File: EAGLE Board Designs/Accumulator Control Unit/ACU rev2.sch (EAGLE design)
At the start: 100 parts, among them J1 CONNECTOR-CAN_NF_T_V_BLACK, J2 CONNECTOR-6_MF_T_V_, J3 CONNECTOR-8_MF_T_V_, Q1 TRANSISTOR_N_MOS__PMV15ENEA, U1 VOLTAGE_REGULATOR_SOT89_12V, U10 OPAMP_1_CHANNEL_OPA991, U11 LOGICGATE_AND_DCK3, U12 OPAMP_1_CHANNEL_OPA991, U13 OPAMP_1_CHANNEL_OPA991, U14 OPAMP_1_CHANNEL_OPA991, U15 LOGICGATE_AND_DCK3, U16 OPAMP_1_CHANNEL_OPA991, U17 OPAMP_1_CHANNEL_OPA991, U18 OPAMP_1_CHANNEL_OPA991, U2 ADG1423, U3 LM555, U4 OPAMP_1_CHANNEL_OPA991, U5 MAX7404, U6 MAX7404, U7 OPAMP_1_CHANNEL_OPA991, U8 LOGICGATE_AND_DCK3, U9 OPAMP_1_CHANNEL_OPA991

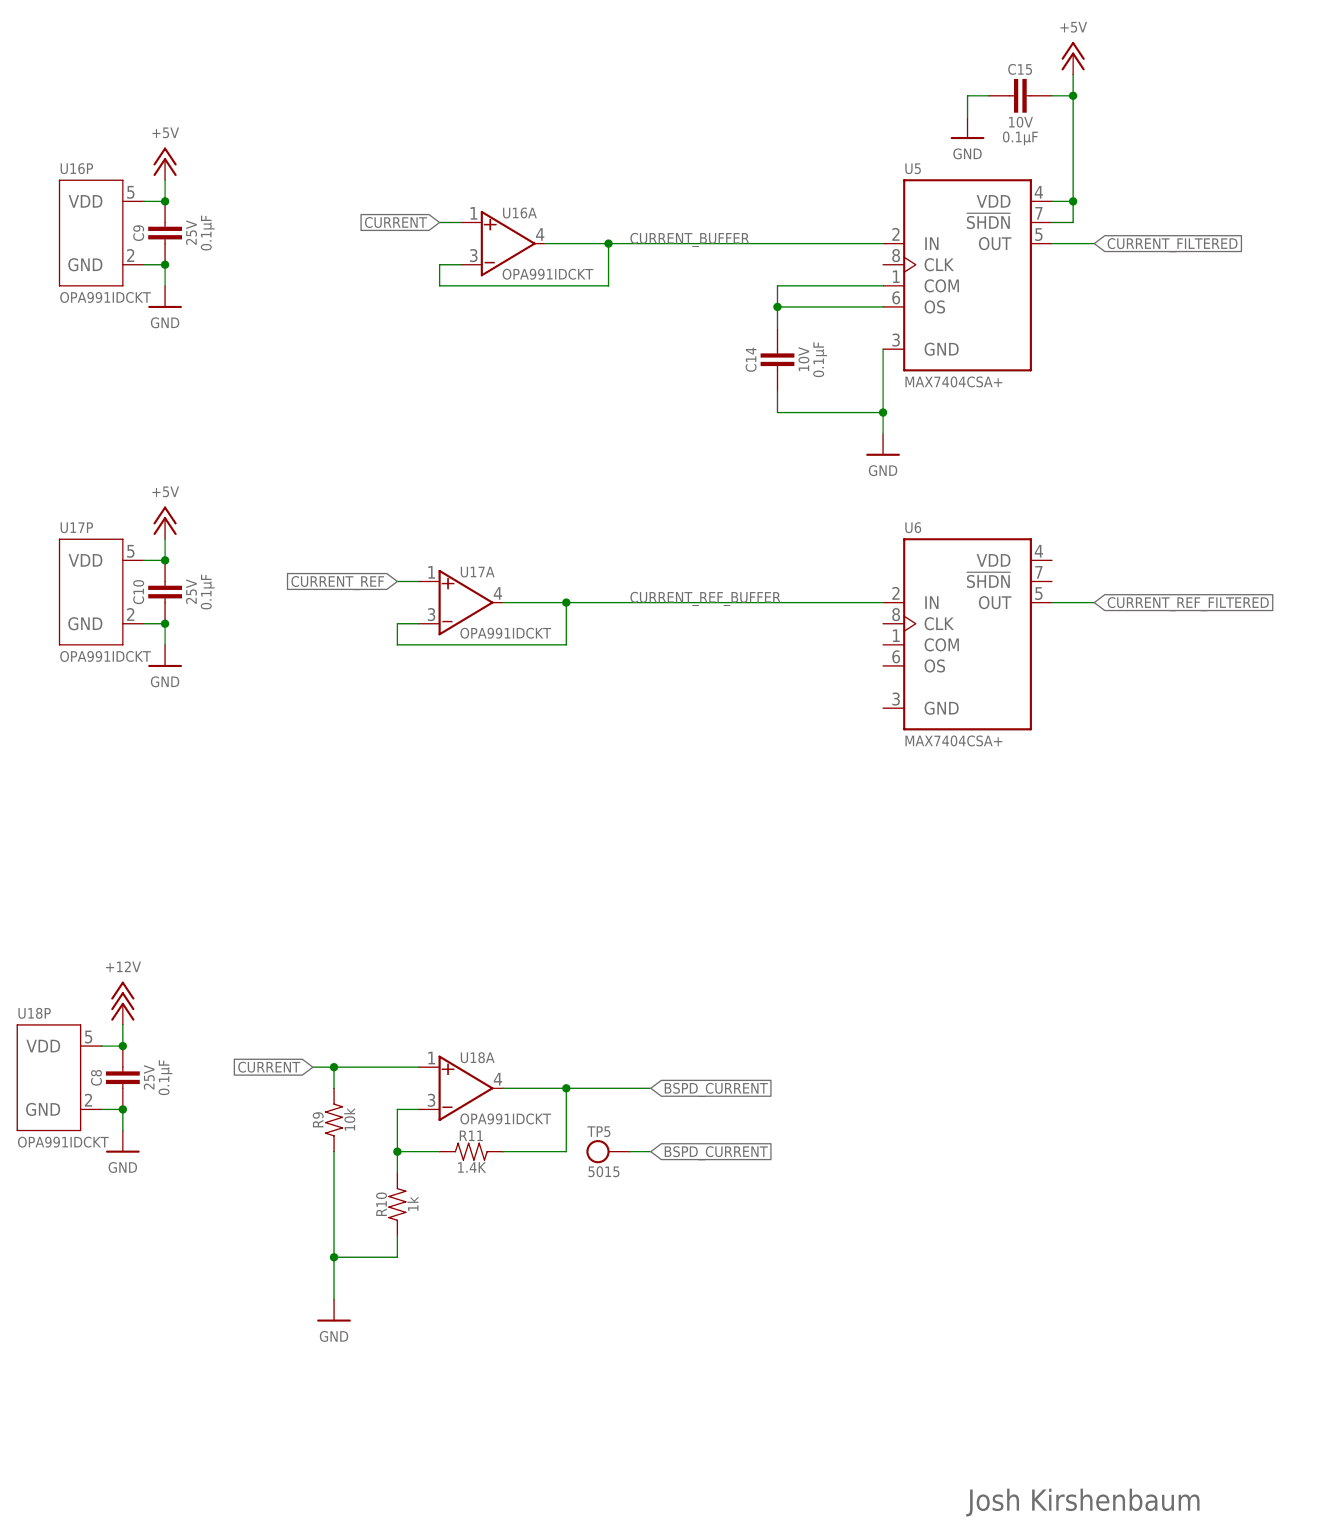
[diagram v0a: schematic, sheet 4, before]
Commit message: filtering capacitor and tvs diode
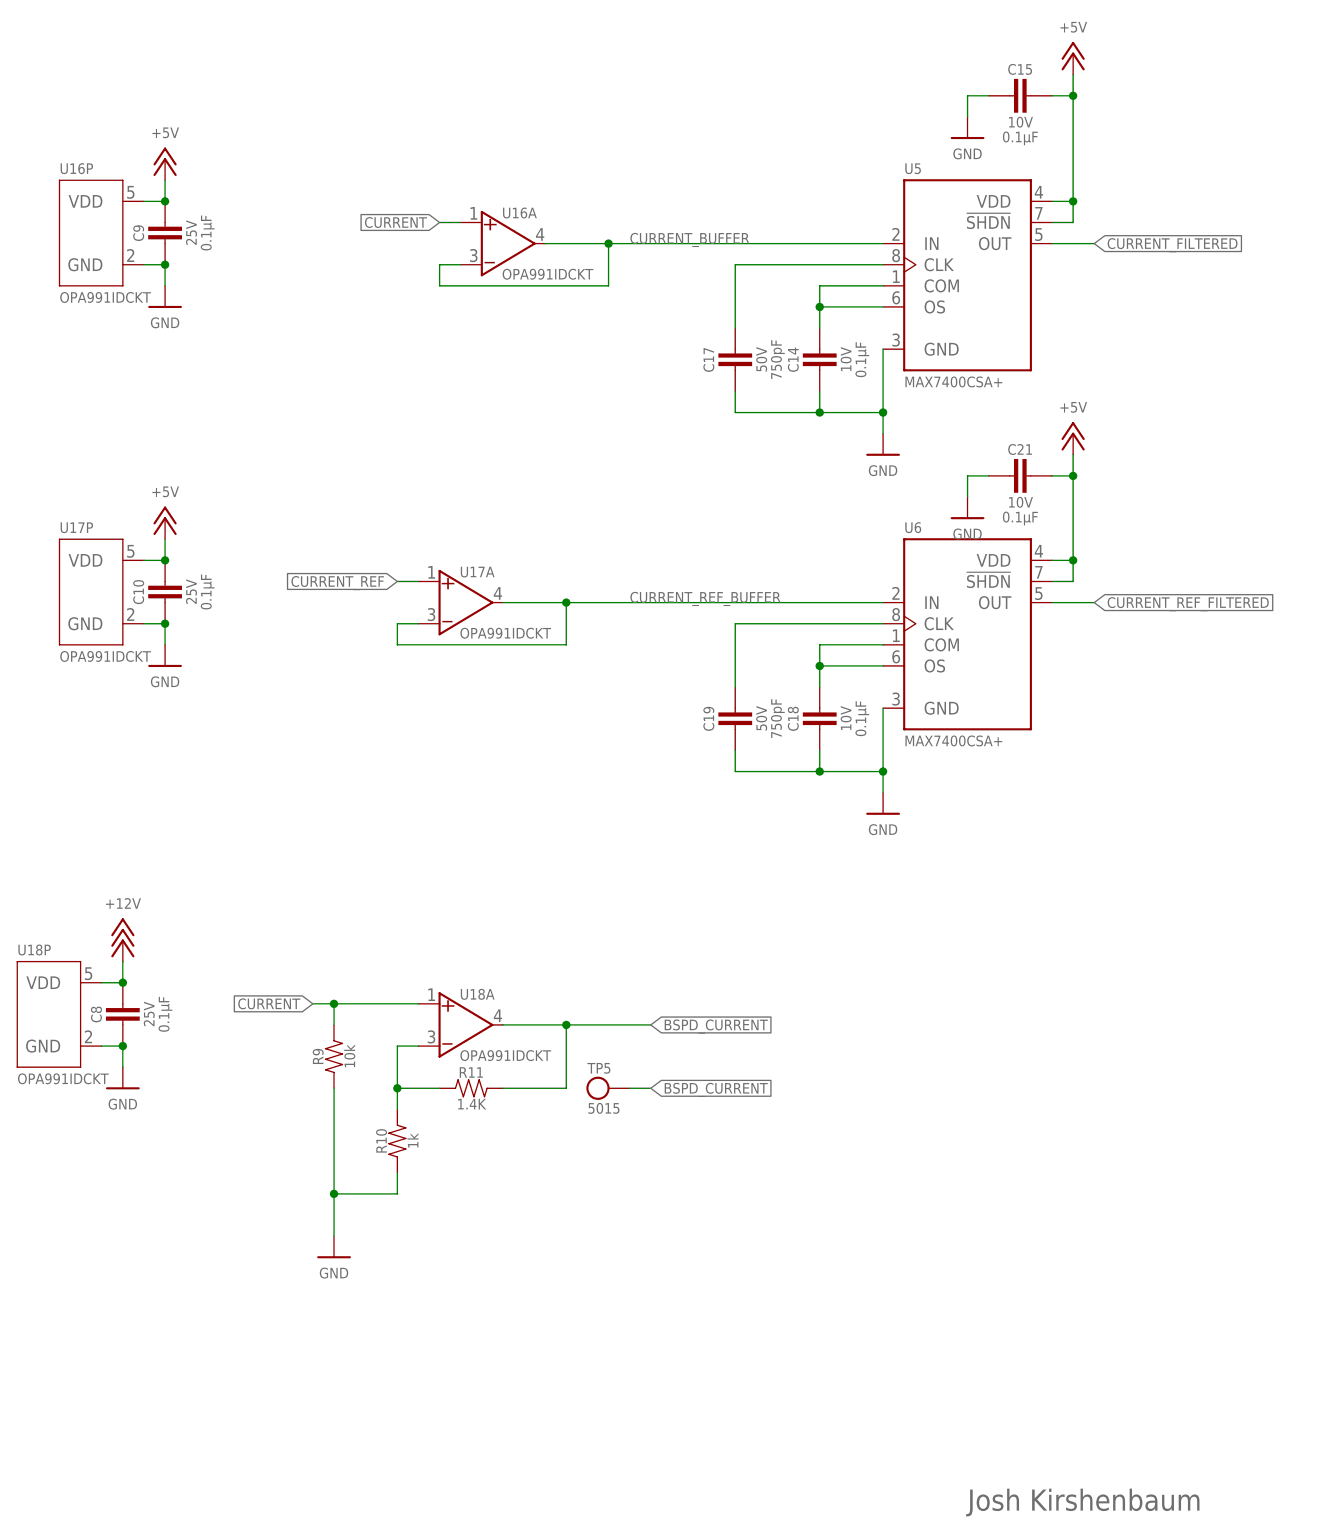
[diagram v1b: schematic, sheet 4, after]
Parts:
- added C17, C19: CAPACITOR_0603_50V_750PF, HyTechDevices - Copy:CAPACITOR_0603_50V_750PF
- added C18, C21: CAPACITOR_0603_10V_0.1UF, HyTechDevices - Copy:CAPACITOR_0603_10V_0.1UF
- added D4: TVS_8V, HyTechDevices - Copy:TVS_8V
- C4: value CAPACITOR_0603_25V_10NF -> CAPACITOR_0603_10V_10NF; device HyTechDevices - Copy:CAPACITOR_0603_25V_10NF -> HyTechDevices - Copy:CAPACITOR_0603_10V_10NF
- C5: value CAPACITOR_0603_25V_4.7UF -> CAPACITOR_0603_10V_4.7NF; device HyTechDevices - Copy:CAPACITOR_0603_25V_4.7UF -> HyTechDevices - Copy:CAPACITOR_0603_10V_4.7NF
- U5, U6: value MAX7404 -> MAX7400; device HyTechDevices:MAX7404 -> HyTechDevices:MAX7400
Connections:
- new net N$14: C17.1, U5.CLK
- new net N$15: C18.1, U6.COM, U6.OS
- new net N$18: C19.1, U6.CLK
- net +5V: now also C21.1, U6.!SHDN, U6.VDD
- net GND: now also C17.2, C18.2, C19.2, C21.2, D4.A, U6.GND
- net PRECHARGE_OK: now also D4.C
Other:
- note added: "Period: 2.834 s Duty Cycle: 50.57%"
- note removed: "TODO SELECT CORRECT TVS DIODE https://www.ti.com/lit/an/slvae37/slvae37.pdf?ts=1635396645786&ref_url=https%253A%252F%252Fwww.google.com%252F"
- moved on the sheet: C14, C8, R10, R11, R9, TP5, U18A, U18P

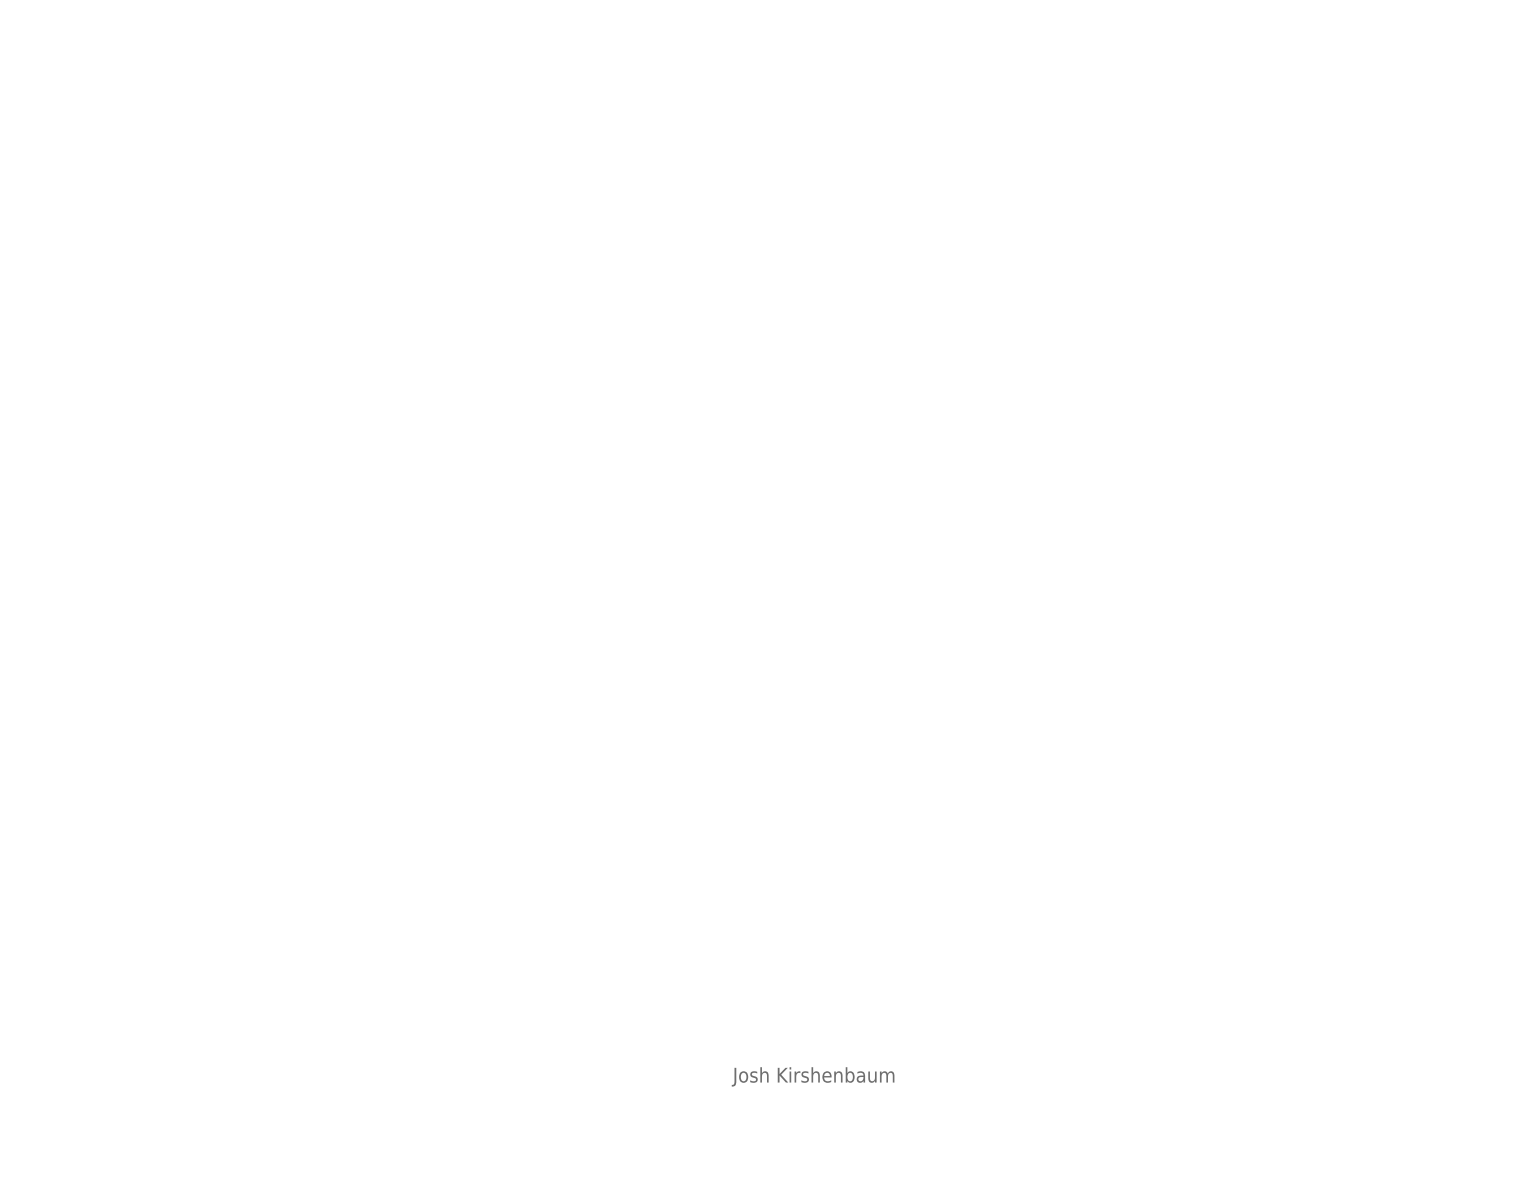
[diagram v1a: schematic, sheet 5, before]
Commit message: teensy adc, watchdog, can
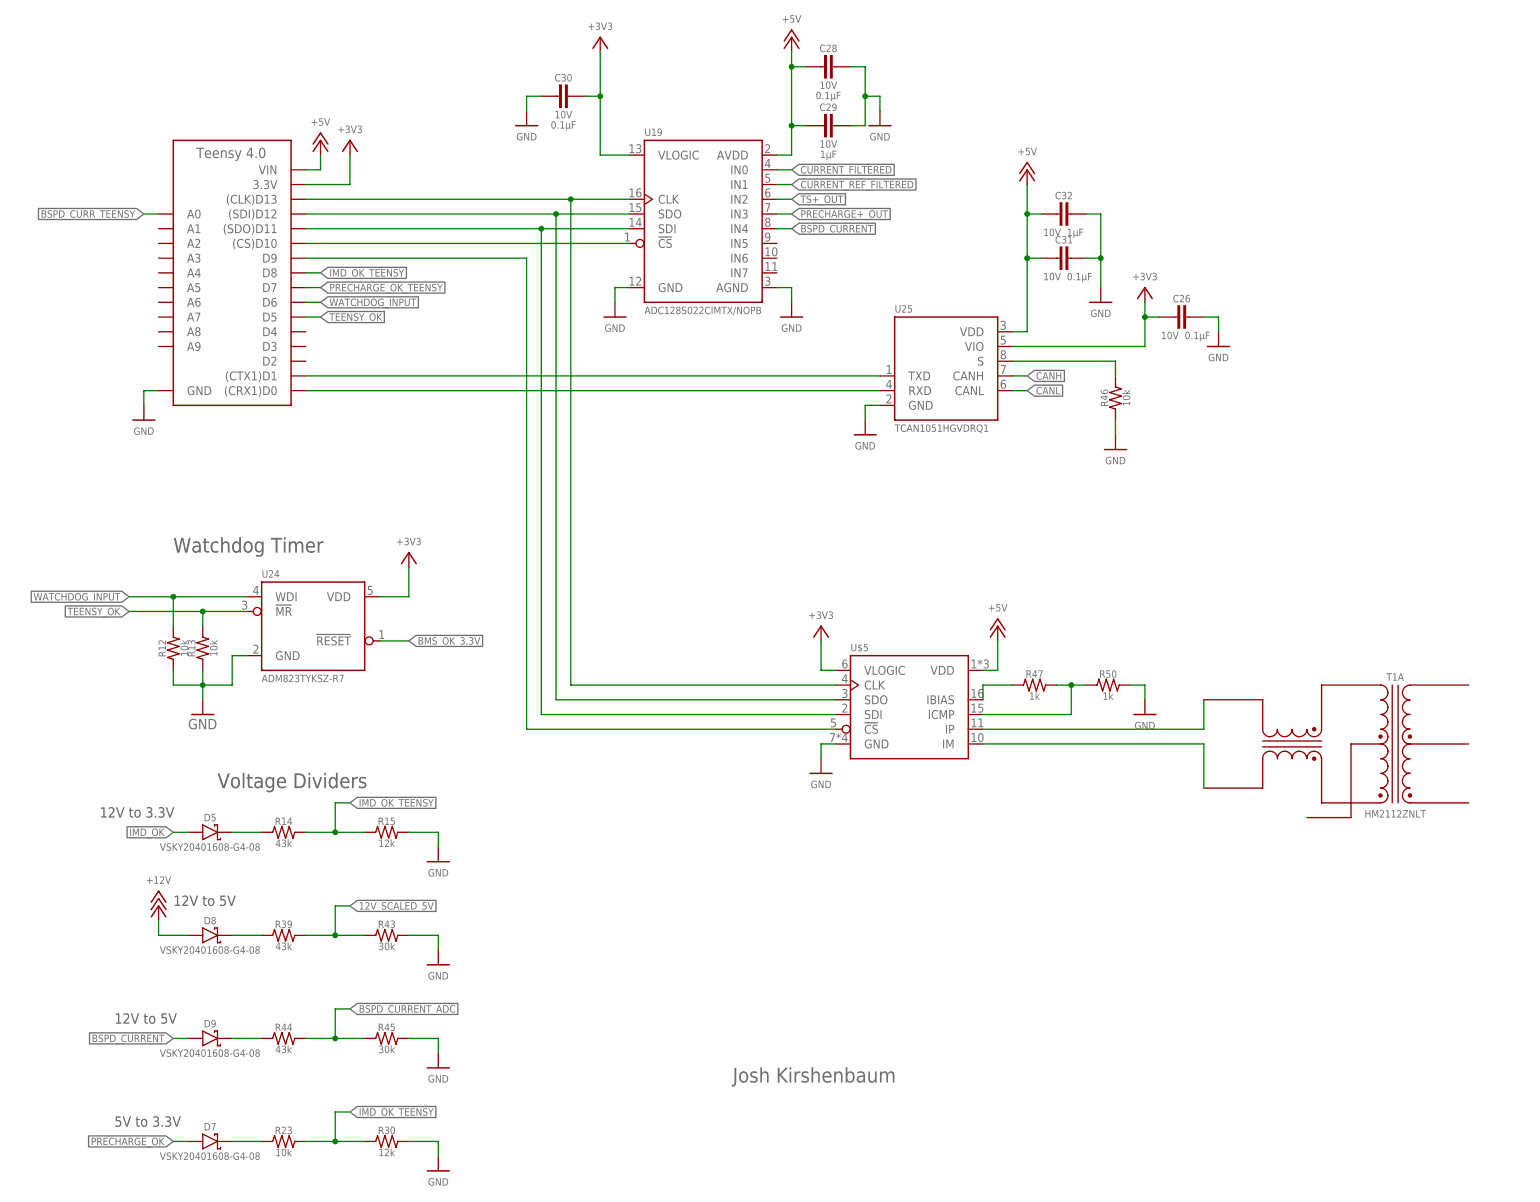
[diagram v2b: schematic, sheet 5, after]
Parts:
- added A1: TEENSY_4.0, HyTechDevices:TEENSY_4.0
- added C26, C31: CAPACITOR_0603_10V_0.1UF, HyTechDevices:CAPACITOR_0603_10V_0.1UF
- added C28, C30: CAPACITOR_0603_10V_0.1UF, HyTechDevices - Copy:CAPACITOR_0603_10V_0.1UF
- added C29: CAPACITOR_0603_10V_1UF, HyTechDevices - Copy:CAPACITOR_0603_10V_1UF
- added C32: CAPACITOR_0603_10V_1UF, HyTechDevices:CAPACITOR_0603_10V_1UF
- added D5, D7, D8, D9: SCHOTTKY, HyTechDevices:SCHOTTKY
- added R12, R13, R46: RESISTOR_0603_10K, HyTechDevices:RESISTOR_0603_10K
- added R14, R39, R44: RESISTOR_0603_43K, HyTechDevices - Copy:RESISTOR_0603_43K
- added R15, R30: RESISTOR_0603_12K, HyTechDevices - Copy:RESISTOR_0603_12K
- added R23: RESISTOR_0603_10K, HyTechDevices - Copy:RESISTOR_0603_10K
- added R43, R45: RESISTOR_0603_30K, HyTechDevices - Copy:RESISTOR_0603_30K
- added R47, R50: RESISTOR_0603_1K, HyTechDevices - Copy:RESISTOR_0603_1K
- added T1: TRANSFORMER_HM2112ZNLT_AIRGAP, HyTechDevices - Copy:TRANSFORMER_HM2112ZNLT_AIRGAP
- added U$5: LTC6820, HyTechDevices - Copy:LTC6820
- added U19: ADC128S022, HyTechDevices - Copy:ADC128S022
- added U24: ADM823, HyTechDevices:ADM823
- added U25: TCAN1051HQV-Q1, HyTechDevices:TCAN1051HQV-Q1
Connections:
- new net +3V3: A1.3.3V, C26.2, C30.1, U$5.VLOGIC, U19.VLOGIC, U24.VDD, U25.VIO
- new net 12V_SCALED_5V: R39.2, R43.1
- new net BSPD_CURRENT_ADC: R44.2, R45.1
- new net BSPD_CURR_TEENSY: A1.A0
- new net CS_LTC_6820: A1.D9, U$5.!CS
- new net IMD_OK_TEENSY: A1.D8, R14.2, R15.1, R23.2, R30.1
- new net N$24: A1.(CTX1)D1, U25.TXD
- new net N$25: A1.(CRX1)D0, U25.RXD
- new net N$26: R46.2, U25.S
- new net N$27: A1.(CLK)D13, U$5.CLK, U19.CLK
- new net N$28: A1.(SDI)D12, U$5.SDO, U19.SDO
- new net N$29: A1.(SDO)D11, U$5.SDI, U19.SDI
- new net N$30: A1.(CS)D10, U19.!CS!
- new net N$31: D7.C, R23.1
- new net N$32: D5.C, R14.1
- new net N$33: D8.C, R39.1
- new net N$34: D9.C, R44.1
- new net N$35: T1A.TD-, U$5.IP
- new net N$36: R47.1, U$5.IBIAS
- new net N$37: R47.2, R50.1, U$5.ICMP
- new net N$38: T1A.TD+, U$5.IM
- new net PRECHARGE_OK_TEENSY: A1.D7
- new net TEENSY_OK: A1.D5, R13.2, U24.!MR!
- new net WATCHDOG_INPUT: A1.D6, R12.2, U24.WDI
- net +12V: now also D8.A
- net +5V: now also A1.VIN, C28.2, C29.2, C31.2, C32.2, U$5.VDD, U19.AVDD, U25.VDD
- net BMS_OK_3.3V: now also U24.!RESET!
- net BSPD_CURRENT: now also D9.A, U19.IN4
- net CANH: now also U25.CANH
- net CANL: now also U25.CANL
- net CURRENT_FILTERED: now also U19.IN0
- net CURRENT_REF_FILTERED: now also U19.IN1
- net GND: now also A1.GND, C26.1, C28.1, C29.1, C30.2, C31.1, C32.1, R12.1, R13.1, R15.2, R30.2, R43.2, R45.2, R46.1, R50.2, U$5.GND, U19.AGND, U19.GND, U24.GND, U25.GND
- net IMD_OK: now also D5.A
- net PRECHARGE+_OUT: now also U19.IN3
- net PRECHARGE_OK: now also D7.A
- net TS+_OUT: now also U19.IN2
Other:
- note added: "12V to 3.3V"
- note added: "12V to 5V"
- note added: "5V to 3.3V"
- note added: "Voltage Dividers"
- note added: "Watchdog Timer"
